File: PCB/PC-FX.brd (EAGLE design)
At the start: 58.5 x 61 mm, 11 parts, among them U1 SN74AHCT125N, U2 SN74AHCT125N

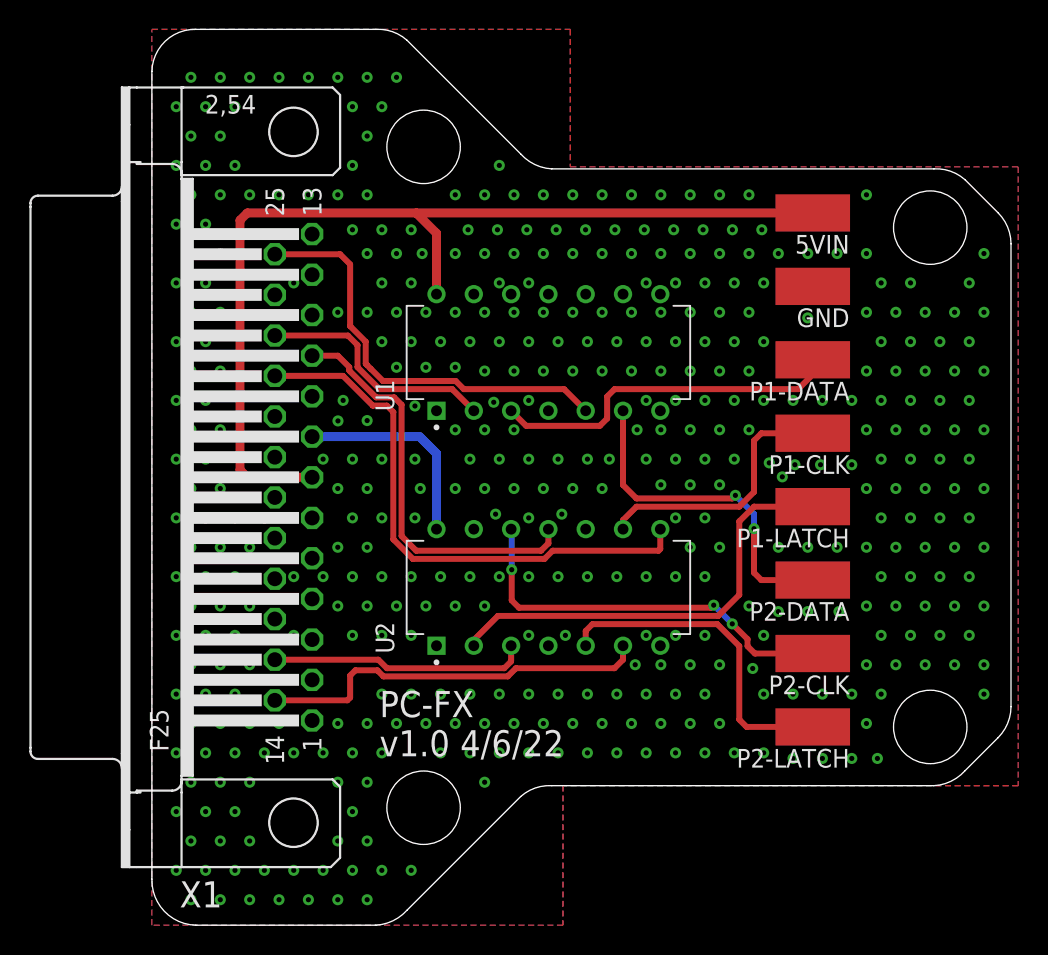
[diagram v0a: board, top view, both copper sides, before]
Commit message: Added exposed GND plane at DB25 anchors
All PCBs have been update to have exposed GND plane pads for the DB25 anchor points.

This resolves Issue 54
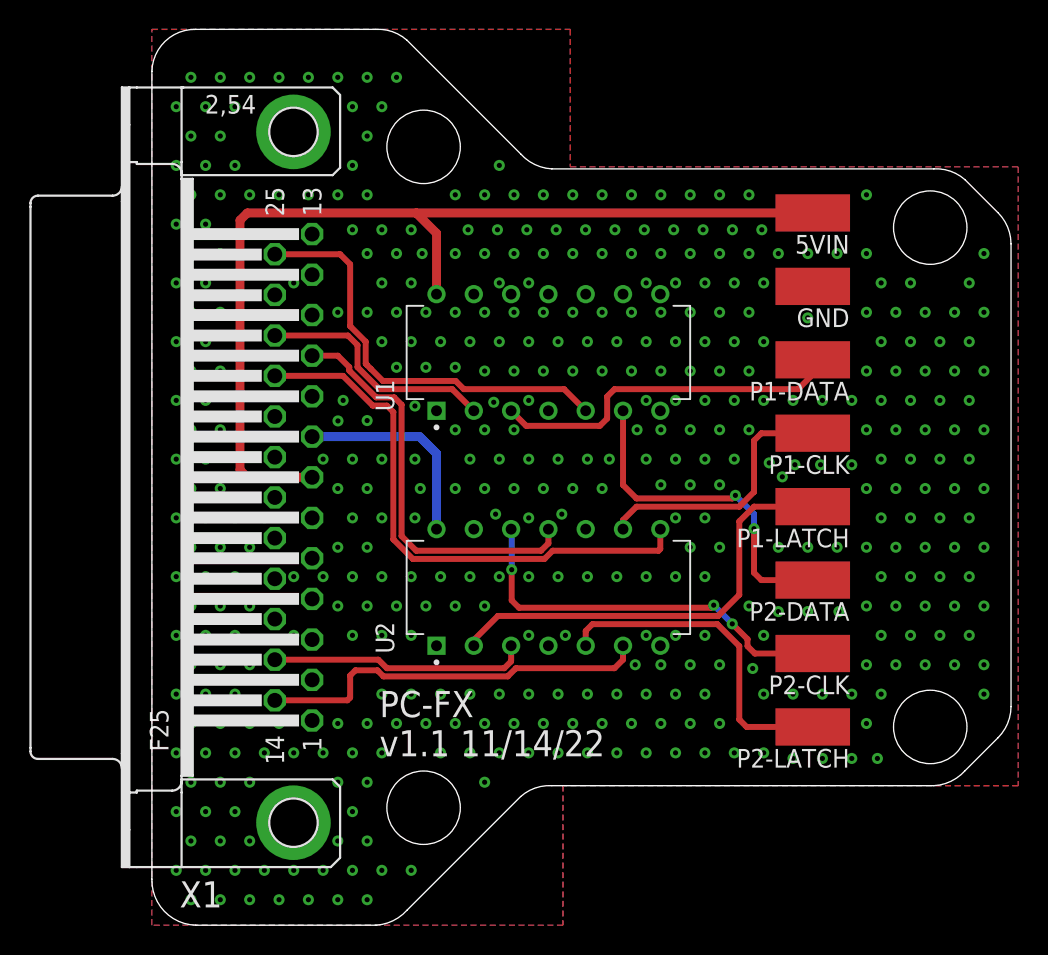
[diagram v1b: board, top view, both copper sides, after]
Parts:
- X1: device SparkFun-Retired:F25H -> SparkFun-Retired:F25HP
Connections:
- net GND: now also X1.GND1, X1.GND2
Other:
- board text added: "PC-FX v1.1 11/14/22"
- board text removed: "PC-FX v1.0 4/6/22"
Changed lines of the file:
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@@
 <hole x="18.5" y="8" drill="5"/>
 <text x="15.5" y="11.5" size="1.778" layer="21">PC-FX
-v1.0 4/6/22</text>
+v1.1 11/14/22</text>
 </plain>
 <attributes>
@@
 <attribute name="PURCHASE-URL" value="https://pricing.snapeda.com/search/part/SN74AHCT125N/?ref=eda" x="65.1" y="47.13" size="1.778" layer="27" rot="R90" display="off"/>
 </element>
-<element name="X1" library="SparkFun-Retired" package="F25H" value="" x="9.64" y="30.5" smashed="yes" rot="R90">
+<element name="X1" library="SparkFun-Retired" package="F25HP" value="" x="9.64" y="30.5" smashed="yes" rot="R90">
 <attribute name="NAME" x="4.789" y="2.99" size="1.778" layer="25" ratio="10" rot="R180"/>
 <attribute name="VALUE" x="-4.33" y="22.118" size="1.778" layer="27" ratio="10" rot="R90"/>
@@
 <via x="55.6568" y="43.735840625" extent="1-16" drill="0.35"/>
 <via x="56.6568" y="45.735840625" extent="1-16" drill="0.35"/>
+<contactref element="X1" pad="GND1"/>
+<contactref element="X1" pad="GND2"/>
 </signal>
 <signal name="5VIN">

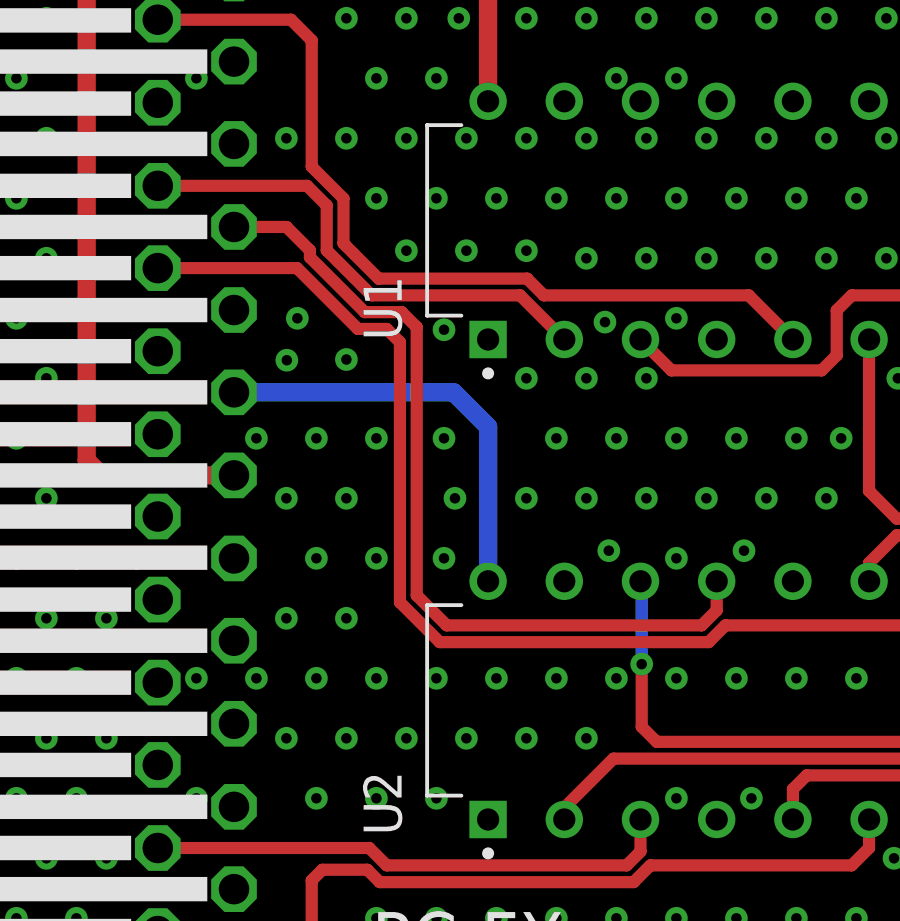
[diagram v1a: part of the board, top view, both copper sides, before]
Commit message: Silkscreen Update, Library Add, Datasheet Add
Updated the silkscreen on all PCBs that used the SN74 components as there was not orientation marker on the silkscreen.

Added Modified SN74 libraries and VB Cable Pinout image
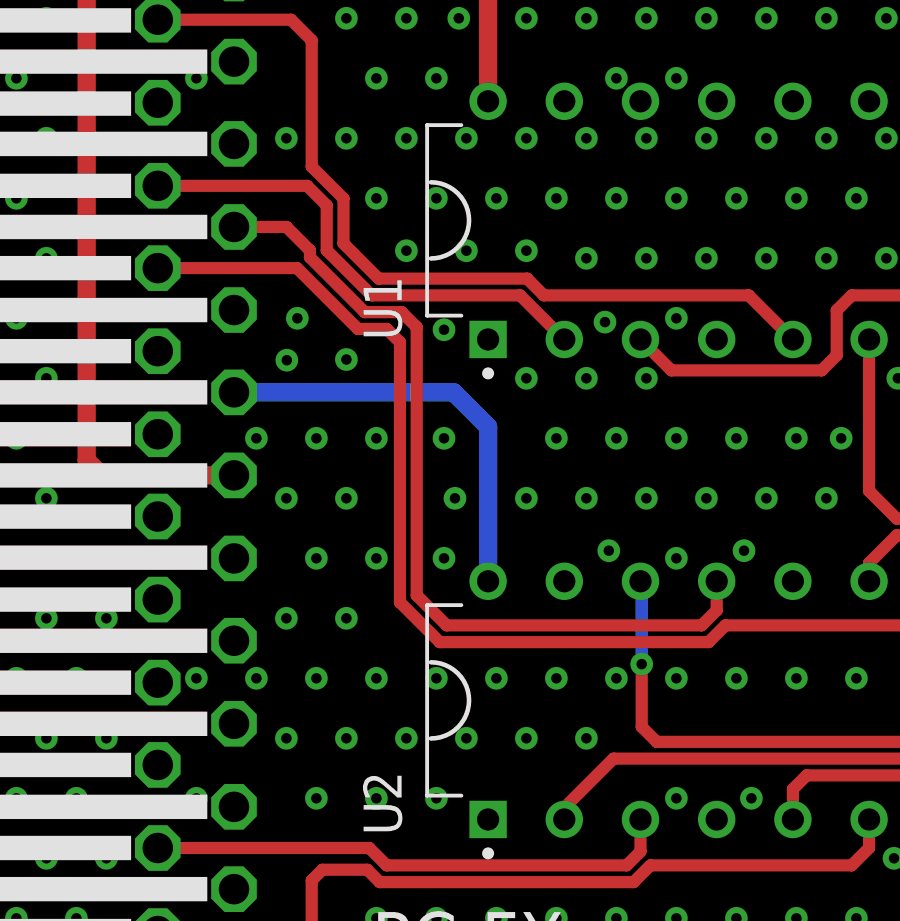
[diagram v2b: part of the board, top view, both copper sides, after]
